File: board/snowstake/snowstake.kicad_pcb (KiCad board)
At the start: 2 copper layers, 76.2 x 91.4 mm, 24 parts, among them Q1 BSS138, Q2 BSS138, U1 PHOTON-MCU_Module

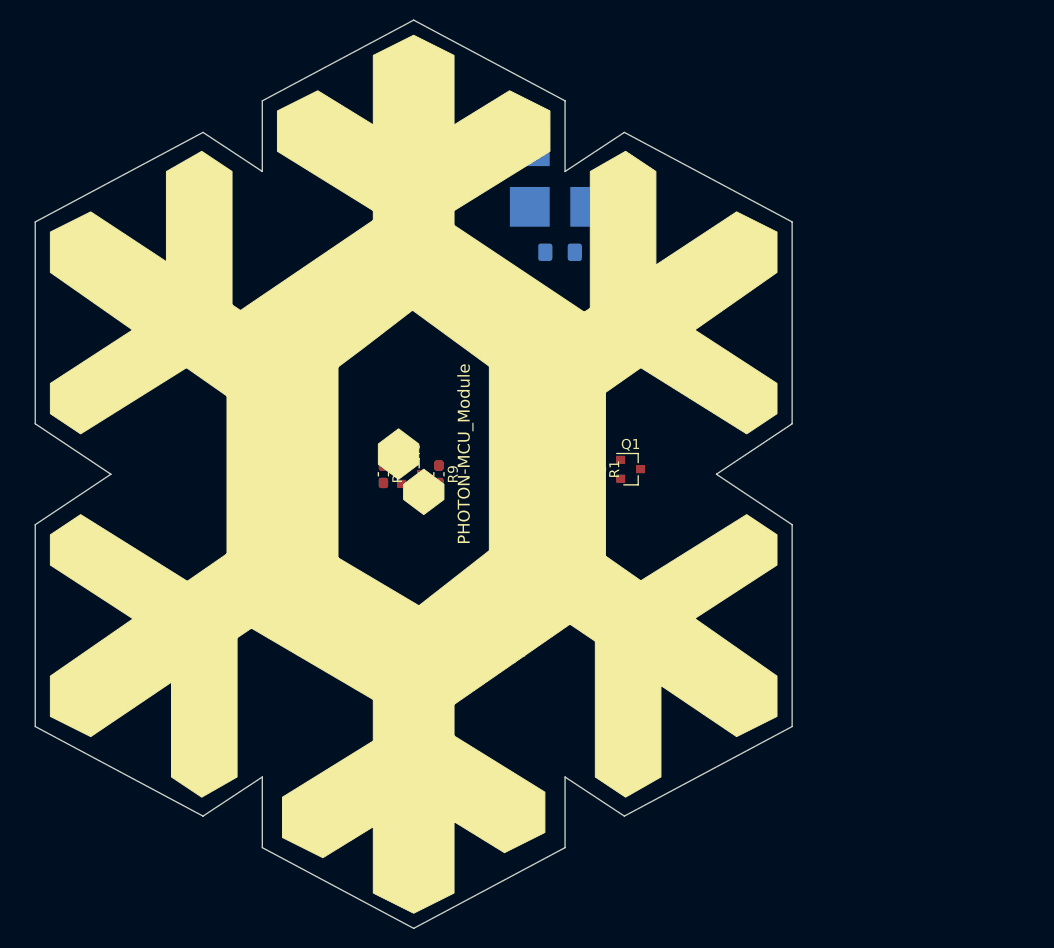
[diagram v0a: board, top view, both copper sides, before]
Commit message: added mounting hole and fiducial
added mounting holes and fiducials to schematic and import to layout
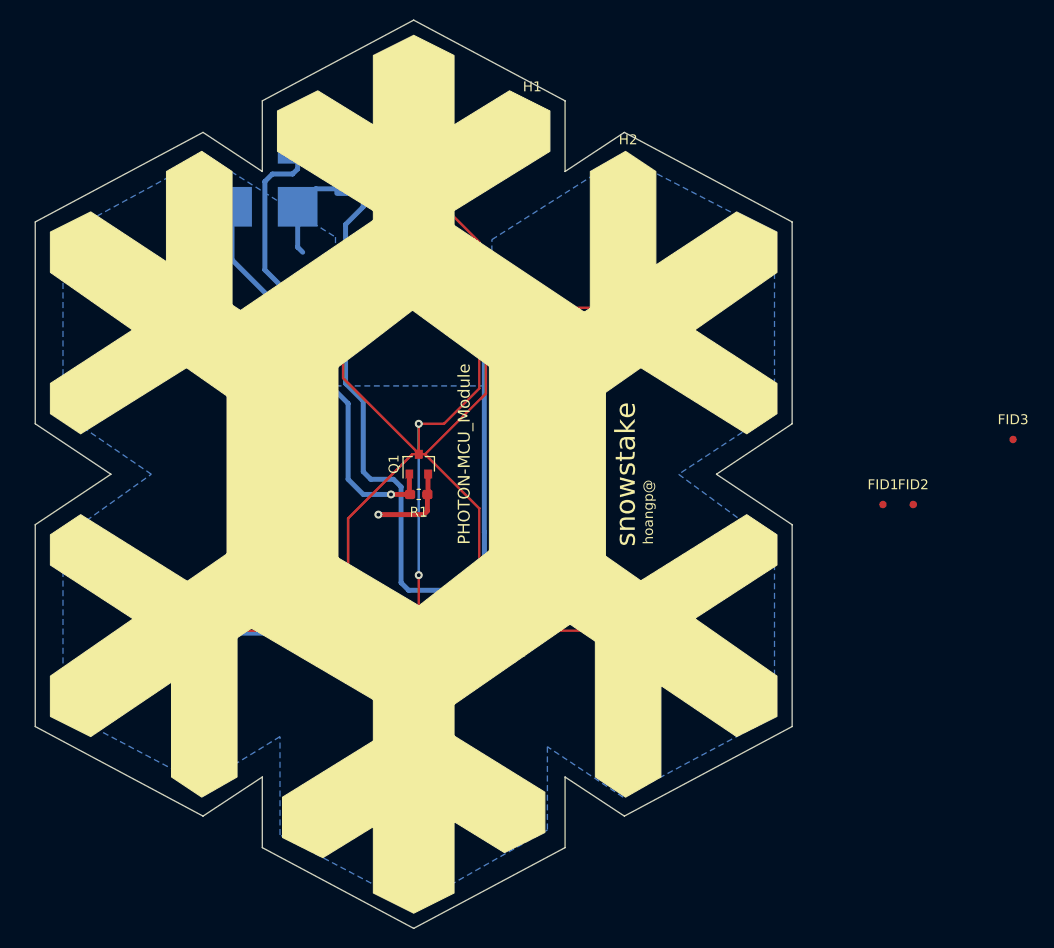
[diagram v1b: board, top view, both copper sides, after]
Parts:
- added FID1: Fiducial, Fiducial:Fiducial_0.75mm_Mask1.5mm, F.Cu at (250.4, 155.4)
- added FID2: Fiducial, Fiducial:Fiducial_0.75mm_Mask1.5mm, F.Cu at (253.5, 155.4)
- added FID3: Fiducial, Fiducial:Fiducial_0.75mm_Mask1.5mm, F.Cu at (263.5, 148.9)
- added H1: MountingHole, MountingHole:MountingHole_2.1mm, F.Cu at (215.1, 116.6)
- added H2: MountingHole, MountingHole:MountingHole_2.1mm, F.Cu at (224.8, 121.9)
- moved TP2 30.6 mm to (184.9, 125.5)
- moved TP1 30.1 mm to (191.5, 119.1)
- moved TP3 23.4 mm to (191.5, 125.5)
- moved C3 23.2 mm to (196.1, 122.2), turned to 270 degrees
- moved Q1 21.3 mm to (203.7, 151.4), turned to 90 degrees
- moved R1 18.5 mm to (203.7, 154.4), turned to 0 degrees
- moved R9 16.3 mm to (190.5, 146.6), turned to 180 degrees
- moved Q2 13.5 mm to (189.7, 149.9), turned to 90 degrees
- moved R6 10.4 mm to (189.7, 152.9), turned to 0 degrees
- moved D4 1.02 mm to (203.2, 113.3)
- turned D1 to 330 degrees
- turned D6 to 30 degrees
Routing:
- net +5V: track 0.00 -> 339.6 mm, vias 0 -> 6
- net Net-(D1-Pad1): track 0.00 -> 281.6 mm, vias 0 -> 2
- net GND: track 0.00 -> 30.4 mm, vias 0 -> 1
- net /DIN: track 0.00 -> 25.4 mm, vias 0 -> 1
- net +3V3: track 0.00 -> 20.0 mm
- net /D2: track 0.00 -> 19.8 mm, vias 0 -> 1
- net /D6: track 0.00 -> 5.87 mm
- net Net-(D5-Pad2): track 0.00 -> 3.78 mm
- net Net-(D6-Pad2): track 0.00 -> 3.42 mm
- net Net-(D1-Pad2): track 0.00 -> 3.42 mm
- net Net-(D3-Pad2): track 0.00 -> 2.46 mm
- net Net-(D2-Pad2): track 0.00 -> 2.28 mm
- net Net-(D4-Pad2): track 0.00 -> 2.25 mm
- added copper zone on B.Cu, net GND
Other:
- board text added: "hoangp@"
- board text added: "snowstake"

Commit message: Updated geometry and generated gerbers
Corrected board geometry to use mathematical angles for hexagon instead of just eye balling it. Generated gerber fabrication files.
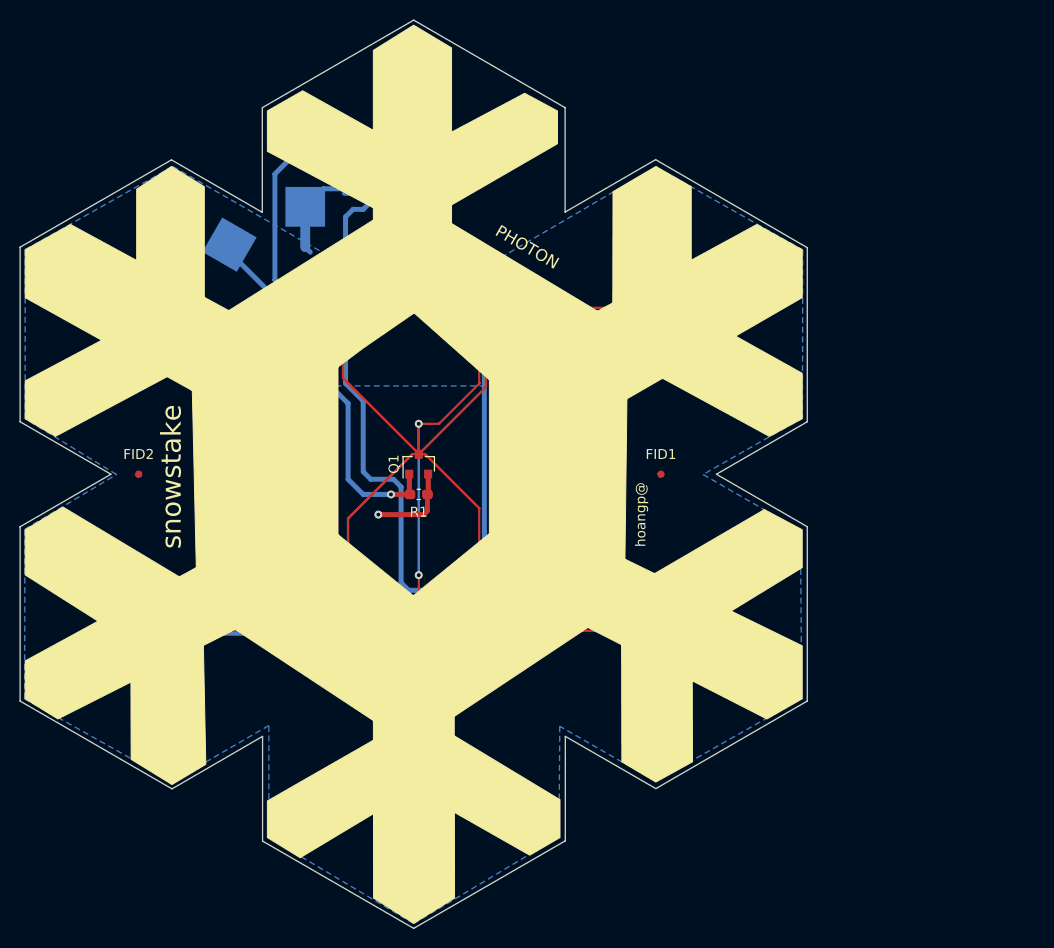
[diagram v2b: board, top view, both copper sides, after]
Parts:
- U1: value PHOTON-MCU_Module -> PHOTON
- moved FID2 78.0 mm to (175.5, 152.4)
- moved FID3 71.0 mm to (197.4, 174.5)
- moved H1 37.3 mm to (178.8, 125.0)
- moved FID1 22.6 mm to (228.1, 152.4)
- moved H2 4.13 mm to (227.6, 125.0)
- moved TP2 3.82 mm to (184.7, 129.3), turned to 60 degrees
- moved D2 3.64 mm to (238.5, 132.1)
- moved R3 3.64 mm to (234.9, 134.1)
- moved D6 3.23 mm to (168.4, 172.5)
- moved R8 3.23 mm to (173.0, 169.9)
- moved D1 2.84 mm to (168.9, 132.6)
- moved R2 2.84 mm to (173.5, 135.1)
- moved D3 2.75 mm to (237.9, 172.5)
- moved R4 2.75 mm to (234.2, 170.4)
- moved C3 0.76 mm to (196.8, 122.2)
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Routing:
- net Net-(D1-Pad1): track 281.6 -> 287.0 mm
- net /DIN: track 25.4 -> 20.6 mm
- net +5V: track 339.6 -> 341.5 mm
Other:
- board size 76.2 x 91.4 mm -> 79.2 x 91.4 mm

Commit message: separated LED control and changed routing
on board LED now have independent control with individual GPIO. Layout updated to clean up routing
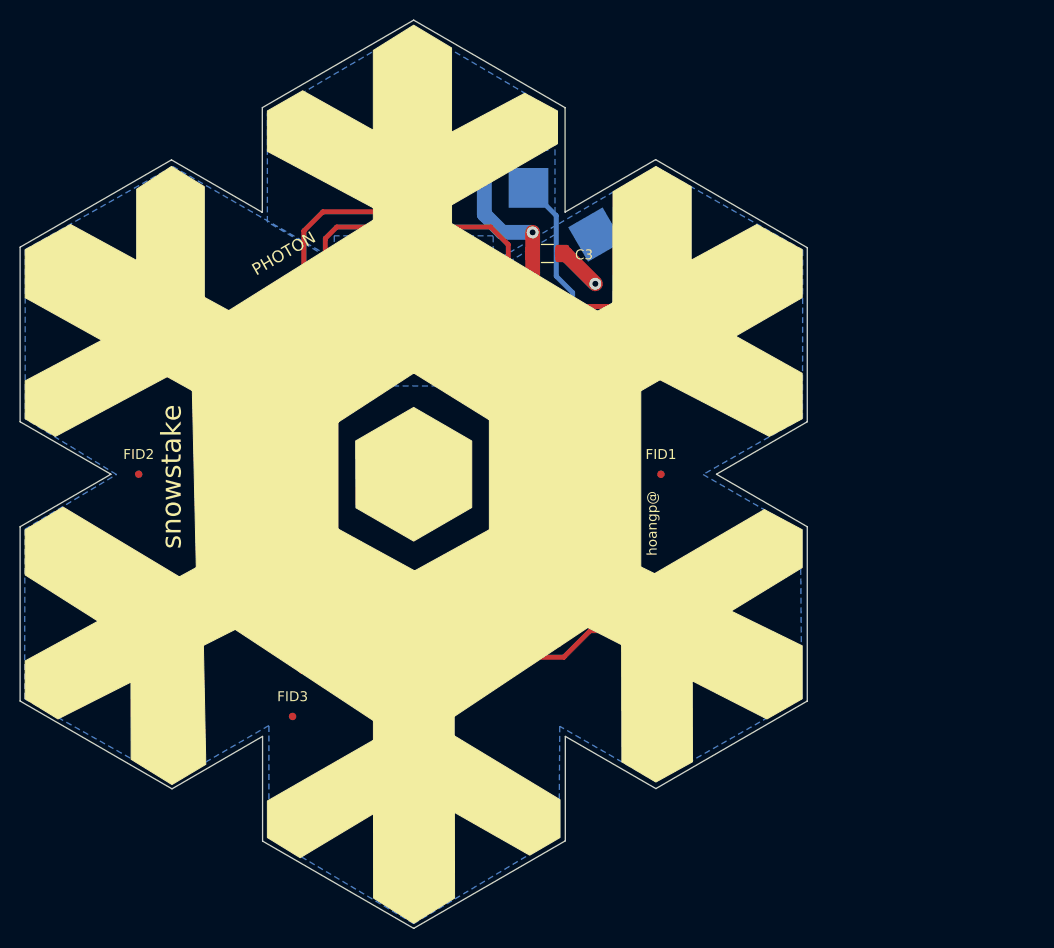
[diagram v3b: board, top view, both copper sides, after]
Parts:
- removed Q1: BSS138, Package_TO_SOT_SMD:SOT-23
- removed R1: 4.99k, Resistor_SMD:R_0603_1608Metric_Pad1.05x0.95mm_HandSolder
- C3: moved to F.Cu
- R2, R3, R4, R5, R7, R8: value 150 -> 499
- moved D3 79.8 mm to (168.8, 132.6), turned to 330 degrees
- moved R4 71.0 mm to (172.7, 134.9), turned to 150 degrees
- moved D6 69.5 mm to (237.9, 172.5), turned to 150 degrees
- moved D1 69.5 mm to (238.4, 132.1), turned to 210 degrees
- moved D4 68.7 mm to (168.4, 172.5), turned to 30 degrees
- moved R2 61.3 mm to (234.8, 134.1), turned to 30 degrees
- moved R5 61.2 mm to (172.2, 170.2), turned to 210 degrees
- moved R8 61.2 mm to (234.2, 170.4), turned to 330 degrees
- moved D2 40.0 mm to (203.2, 113.3), turned to 270 degrees
- moved R3 36.1 mm to (203.2, 117.0), turned to 90 degrees
- moved TP2 30.6 mm to (214.8, 123.6), turned to 0 degrees
- moved Q2 29.9 mm to (219.6, 151.3)
- moved R6 29.9 mm to (219.6, 154.3)
- moved TP3 29.3 mm to (221.5, 128.3), turned to 30 degrees
- moved R9 28.2 mm to (218.7, 147.8), turned to 0 degrees
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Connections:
- D1 pad 1: Net-(D1-Pad1) -> GND
- D2 pad 1: Net-(D1-Pad1) -> GND
- D3 pad 1: Net-(D1-Pad1) -> GND
- D4 pad 1: Net-(D1-Pad1) -> GND
- D5 pad 1: Net-(D1-Pad1) -> GND
- D6 pad 1: Net-(D1-Pad1) -> GND
- R2 pad 1: +5V -> /D0
- R3 pad 1: +5V -> /D1
- R4 pad 1: +5V -> /D2
- R5 pad 1: +5V -> /D3
- R7 pad 1: +5V -> /D4
- R8 pad 1: +5V -> /D5
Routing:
- net Net-(D1-Pad1): track 287.0 -> 0.00 mm, vias 2 -> 0
- net +5V: track 341.5 -> 69.7 mm, vias 6 -> 1
- net /D5: track 0.00 -> 69.3 mm
- net /D6: track 5.87 -> 64.4 mm
- net /D0: track 0.00 -> 56.0 mm, vias 0 -> 2
- net /D4: track 0.00 -> 53.1 mm
- net /D3: track 0.00 -> 39.3 mm
- net /D1: track 0.00 -> 33.6 mm
- net +3V3: track 20.0 -> 45.0 mm
- net /DIN: track 20.6 -> 29.8 mm
- net GND: track 30.4 -> 25.6 mm, vias 1 -> 7
- net /D2: track 19.8 -> 22.9 mm, vias 1 -> 0
- net Net-(D1-Pad2): track 3.42 -> 2.28 mm
- net Net-(D6-Pad2): track 3.42 -> 2.46 mm
